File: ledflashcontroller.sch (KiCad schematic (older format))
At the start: 23 parts, among them J1 CONN_01X02, J2 CONN_01X02, J3 Conn_02x08_Odd_Even, K1 LDD-1000H, K2 LDD-1000H, P1 V_DIM1, P2 V_DIM2, P3 V_OUT, P4 I2C_HEADER, P5 GPIO_HEADER, P6 V_IN, Q1 IRLML6244, Q2 IRFB3256, U1 Teensy3.6

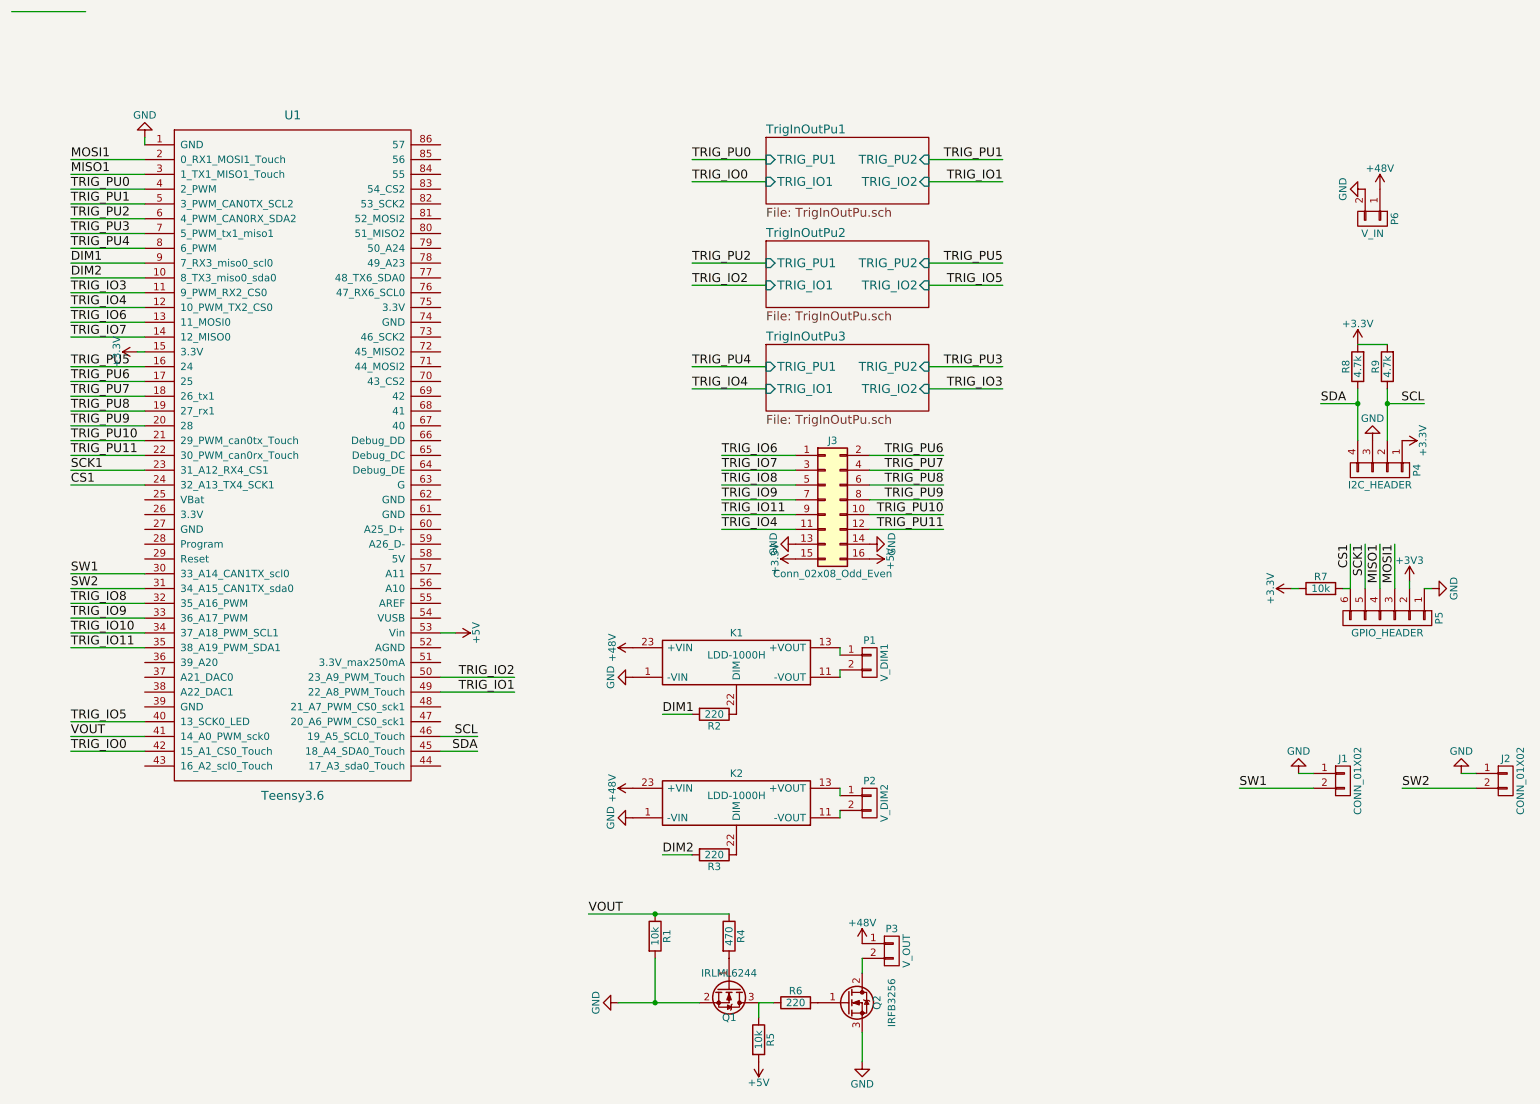
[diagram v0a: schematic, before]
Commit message: Fixed some annotations and footprints
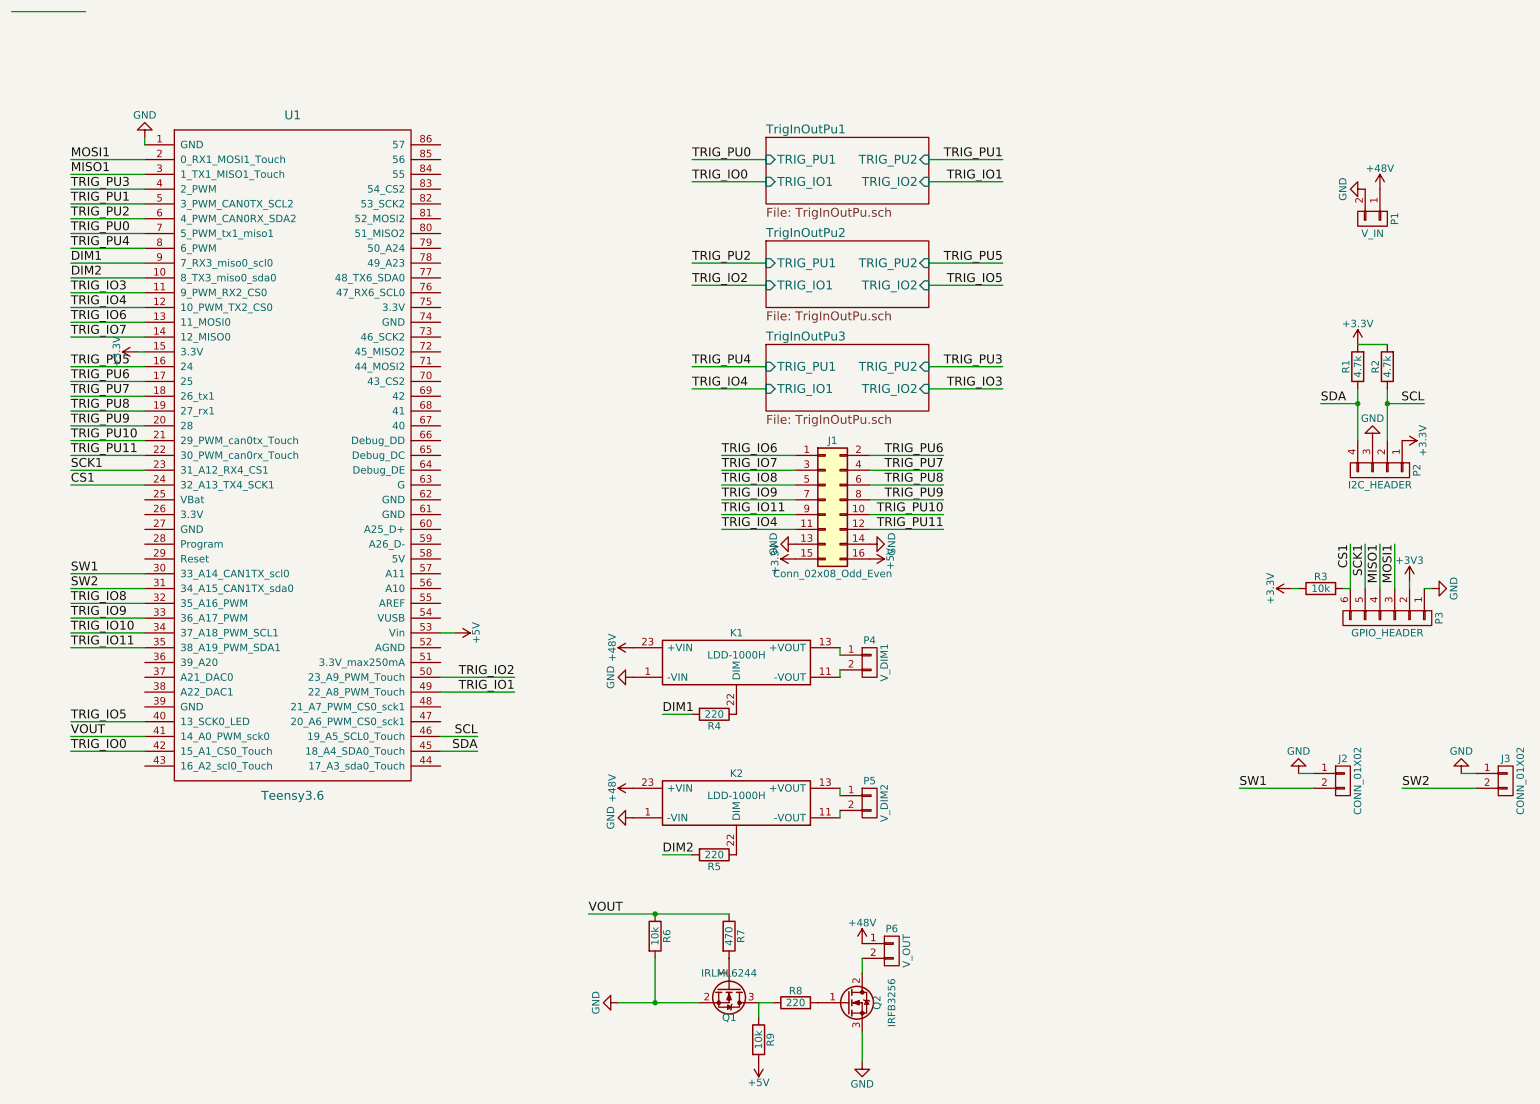
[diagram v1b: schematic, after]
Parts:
- J1: renamed from J3; footprint Pin_Headers:Pin_Header_Straight_2x08_Pitch1.00mm -> Pin_Headers:Pin_Header_Straight_2x08_Pitch2.54mm_SMD
- P3: renamed from P5; footprint Pin_Headers:Pin_Header_Straight_1x04_Pitch2.54mm -> Pin_Headers:Pin_Header_Straight_1x06_Pitch2.54mm
- renumbered J1 to J2, J2 to J3, P6 to P1, P4 to P2, P1 to P4, P2 to P5, P3 to P6, R8 to R1, R9 to R2, R7 to R3, R2 to R4, R3 to R5, R1 to R6, R4 to R7, R6 to R8, R5 to R9
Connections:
- net TRIG_PU0: now also U1.7 (5_PWM_tx1_miso1); no longer U1.4 (2_PWM)
- net TRIG_PU3: now also U1.4 (2_PWM); no longer U1.7 (5_PWM_tx1_miso1)
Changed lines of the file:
@@
 $EndComp
 $Comp
-L R R9
+L R R2
 U 1 1 5981ADF0
 P 9650 2450
-F 0 "R9" V 9730 2450 50  0000 C CNN
+F 0 "R2" V 9730 2450 50  0000 C CNN
 F 1 "4.7k" V 9650 2450 50  0000 C CNN
 F 2 "Resistors_SMD:R_1206_HandSoldering" V 9580 2450 50  0001 C CNN
@@
 $EndComp
 $Comp
-L R R8
+L R R1
 U 1 1 5981AE6C
 P 9450 2450
-F 0 "R8" V 9530 2450 50  0000 C CNN
+F 0 "R1" V 9530 2450 50  0000 C CNN
 F 1 "4.7k" V 9450 2450 50  0000 C CNN
 F 2 "Resistors_SMD:R_1206_HandSoldering" V 9380 2450 50  0001 C CNN
@@
 SCL
 $Comp
-L CONN_01X04 P4
+L CONN_01X04 P2
 U 1 1 5981B195
 P 9600 3150
-F 0 "P4" H 9600 3400 50  0000 C CNN
+F 0 "P2" H 9600 3400 50  0000 C CNN
 F 1 "I2C_HEADER" V 9700 3150 50  0000 C CNN
 F 2 "Pin_Headers:Pin_Header_Straight_1x04_Pitch2.54mm" H 9600 3150 50  0001 C CNN
@@
 SW2
 $Comp
-L CONN_01X02 P3
+L CONN_01X02 P6
 U 1 1 59820649
 P 6300 6400
-F 0 "P3" H 6300 6550 50  0000 C CNN
+F 0 "P6" H 6300 6550 50  0000 C CNN
 F 1 "V_OUT" V 6400 6400 50  0000 C CNN
 F 2 "lib_fp:DELTRON_571_x2" H 6300 6400 50  0001 C CNN
@@
 DIM1
 $Comp
-L CONN_01X02 P1
+L CONN_01X02 P4
 U 1 1 59824324
 P 6150 4450
-F 0 "P1" H 6150 4600 50  0000 C CNN
+F 0 "P4" H 6150 4600 50  0000 C CNN
 F 1 "V_DIM1" V 6250 4450 50  0000 C CNN
 F 2 "lib_fp:DELTRON_571_x2" H 6150 4450 50  0001 C CNN
@@
 DIM2
 $Comp
-L CONN_01X02 P2
+L CONN_01X02 P5
 U 1 1 5982447B
 P 6150 5400
-F 0 "P2" H 6150 5550 50  0000 C CNN
+F 0 "P5" H 6150 5550 50  0000 C CNN
 F 1 "V_DIM2" V 6250 5400 50  0000 C CNN
 F 2 "lib_fp:DELTRON_571_x2" H 6150 5400 50  0001 C CNN
@@
 CS1
 $Comp
-L CONN_01X06 P5
+L CONN_01X06 P3
 U 1 1 59825F8A
 P 9650 4150
-F 0 "P5" H 9650 4500 50  0000 C CNN
+F 0 "P3" H 9650 4500 50  0000 C CNN
 F 1 "GPIO_HEADER" V 9750 4150 50  0000 C CNN
-F 2 "Pin_Headers:Pin_Header_Straight_1x04_Pitch2.54mm" H 9650 4150 50  0001 C CNN
+F 2 "Pin_Headers:Pin_Header_Straight_1x06_Pitch2.54mm" H 9650 4150 50  0001 C CNN
 F 3 "" H 9650 4150 50  0000 C CNN
 	1    9650 4150
@@
 CS1
 $Comp
-L R R2
+L R R4
 U 1 1 5981D11F
 P 5100 4800
-F 0 "R2" V 5180 4800 50  0000 C CNN
+F 0 "R4" V 5180 4800 50  0000 C CNN
 F 1 "220" V 5100 4800 50  0000 C CNN
 F 2 "Resistors_SMD:R_1206_HandSoldering" V 5030 4800 50  0001 C CNN
@@
 $EndComp
 $Comp
-L CONN_01X02 P6
+L CONN_01X02 P1
 U 1 1 5992C559
 P 9550 1450
-F 0 "P6" H 9550 1600 50  0000 C CNN
+F 0 "P1" H 9550 1600 50  0000 C CNN
 F 1 "V_IN" V 9650 1450 50  0000 C CNN
 F 2 "lib_fp:DELTRON_571_x2" H 9550 1450 50  0001 C CNN
@@
 $EndComp
 $Comp
-L R R3
+L R R5
 U 1 1 5995EFDE
 P 5100 5750
-F 0 "R3" V 5180 5750 50  0000 C CNN
+F 0 "R5" V 5180 5750 50  0000 C CNN
 F 1 "220" V 5100 5750 50  0000 C CNN
 F 2 "Resistors_SMD:R_1206_HandSoldering" V 5030 5750 50  0001 C CNN
@@
 	5950 5450 5950 5500
 $Comp
-L R R1
+L R R6
 U 1 1 599C3A5A
 P 4700 6300
-F 0 "R1" V 4780 6300 50  0000 C CNN
+F 0 "R6" V 4780 6300 50  0000 C CNN
 F 1 "10k" V 4700 6300 50  0000 C CNN
 F 2 "Resistors_SMD:R_1206_HandSoldering" V 4630 6300 50  0001 C CNN
@@
 $EndComp
 $Comp
-L R R4
+L R R7
 U 1 1 599C3A60
 P 5200 6300
-F 0 "R4" V 5280 6300 50  0000 C CNN
+F 0 "R7" V 5280 6300 50  0000 C CNN
 F 1 "470" V 5200 6300 50  0000 C CNN
 F 2 "Resistors_SMD:R_1206_HandSoldering" V 5130 6300 50  0001 C CNN
@@
 $EndComp
 $Comp
-L R R5
+L R R9
 U 1 1 599C3A6D
 P 5400 7000
-F 0 "R5" V 5480 7000 50  0000 C CNN
+F 0 "R9" V 5480 7000 50  0000 C CNN
 F 1 "10k" V 5400 7000 50  0000 C CNN
 F 2 "Resistors_SMD:R_1206_HandSoldering" V 5330 7000 50  0001 C CNN
@@
 	4450 6750 5000 6750
 $Comp
-L R R6
+L R R8
 U 1 1 599C3A7D
 P 5650 6750
-F 0 "R6" V 5730 6750 50  0000 C CNN
+F 0 "R8" V 5730 6750 50  0000 C CNN
 F 1 "220" V 5650 6750 50  0000 C CNN
 F 2 "Resistors_SMD:R_1206_HandSoldering" V 5580 6750 50  0001 C CNN
@@
 	5400 6850 5400 6750
 $Comp
-L CONN_01X02 J1
+L CONN_01X02 J2
 U 1 1 59AA3763
 P 9350 5250
-F 0 "J1" H 9350 5400 50  0000 C CNN
+F 0 "J2" H 9350 5400 50  0000 C CNN
 F 1 "CONN_01X02" V 9450 5250 50  0000 C CNN
 F 2 "Pin_Headers:Pin_Header_Straight_1x02_Pitch2.54mm" H 9350 5250 50  0001 C CNN
@@
 $EndComp
 $Comp
-L CONN_01X02 J2
+L CONN_01X02 J3
 U 1 1 59AA3819
 P 10450 5250
-F 0 "J2" H 10450 5400 50  0000 C CNN
+F 0 "J3" H 10450 5400 50  0000 C CNN
 F 1 "CONN_01X02" V 10550 5250 50  0000 C CNN
 F 2 "Pin_Headers:Pin_Header_Straight_1x02_Pitch2.54mm" H 10450 5250 50  0001 C CNN
@@
 	9750 5300 10250 5300
 $Comp
-L R R7
+L R R3
 U 1 1 59AA62D1
 P 9200 3950
-F 0 "R7" V 9280 3950 50  0000 C CNN
+F 0 "R3" V 9280 3950 50  0000 C CNN
 F 1 "10k" V 9200 3950 50  0000 C CNN
 F 2 "Resistors_SMD:R_1206_HandSoldering" V 9130 3950 50  0001 C CNN
@@
 	1250 1450 750  1450
 Text Label 750  1250 0    60   ~ 0
-TRIG_PU0
+TRIG_PU3
 Text Label 750  1350 0    60   ~ 0
 TRIG_PU1
@@
 TRIG_PU2
 Text Label 750  1550 0    60   ~ 0
-TRIG_PU3
+TRIG_PU0
 Wire Wire Line
 	1250 1650 750  1650
@@
 TRIG_IO1
 $Comp
-L Conn_02x08_Odd_Even J3
+L Conn_02x08_Odd_Even J1
 U 1 1 59B82D2A
 P 5850 3350
-F 0 "J3" H 5900 3750 50  0000 C CNN
+F 0 "J1" H 5900 3750 50  0000 C CNN
 F 1 "Conn_02x08_Odd_Even" H 5900 2850 50  0000 C CNN
-F 2 "Pin_Headers:Pin_Header_Straight_2x08_Pitch1.00mm" H 5850 3350 50  0001 C CNN
+F 2 "Pin_Headers:Pin_Header_Straight_2x08_Pitch2.54mm_SMD" H 5850 3350 50  0001 C CNN
 F 3 "" H 5850 3350 50  0001 C CNN
 	1    5850 3350

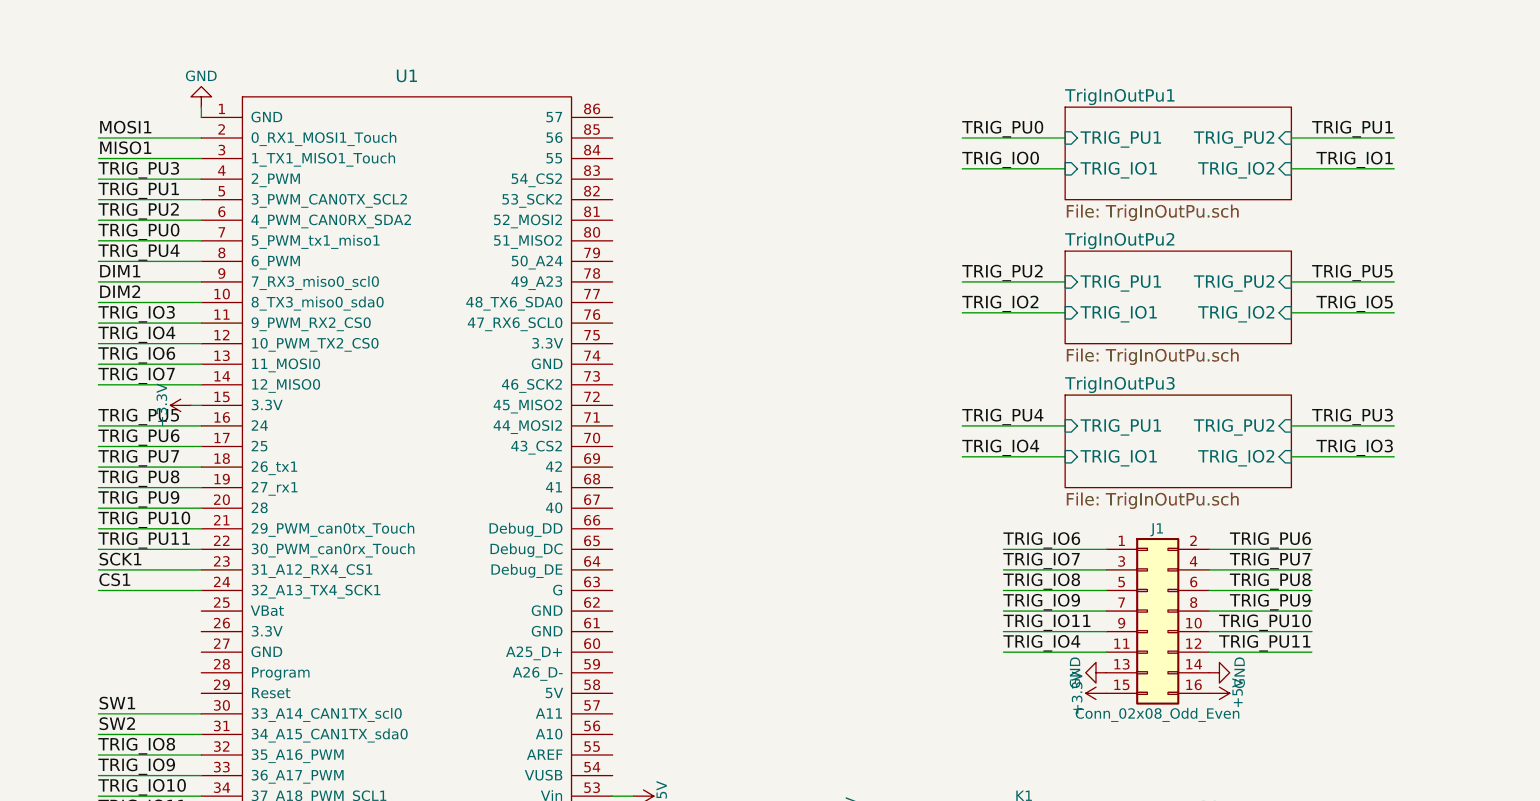
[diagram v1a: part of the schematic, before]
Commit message: Bugfixes for vias to close to wires
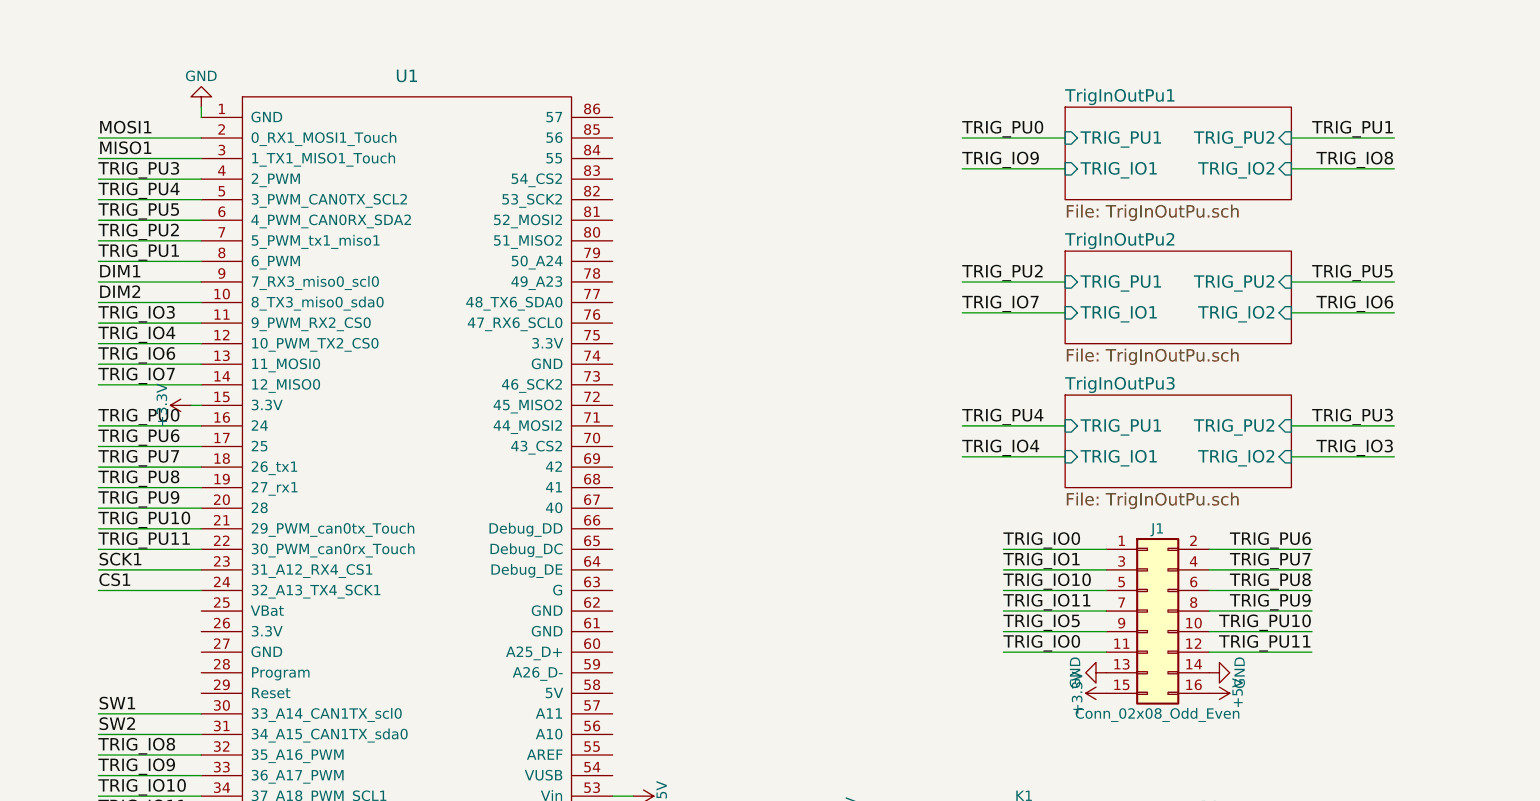
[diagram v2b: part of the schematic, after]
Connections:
- net TRIG_IO0: now also J1.1 (Pin_1), J1.11 (Pin_11)
- net TRIG_IO1: now also J1.3 (Pin_3)
- net TRIG_IO10: now also J1.5 (Pin_5)
- net TRIG_IO11: now also J1.7 (Pin_7); no longer J1.9 (Pin_9)
- net TRIG_IO4: no longer J1.11 (Pin_11)
- net TRIG_IO5: now also J1.9 (Pin_9)
- net TRIG_IO6: no longer J1.1 (Pin_1)
- net TRIG_IO7: no longer J1.3 (Pin_3)
- net TRIG_IO8: no longer J1.5 (Pin_5)
- net TRIG_IO9: no longer J1.7 (Pin_7)
- net TRIG_PU0: now also U1.16 (24); no longer U1.7 (5_PWM_tx1_miso1)
- net TRIG_PU1: now also U1.8 (6_PWM); no longer U1.5 (3_PWM_CAN0TX_SCL2)
- net TRIG_PU2: now also U1.7 (5_PWM_tx1_miso1); no longer U1.6 (4_PWM_CAN0RX_SDA2)
- net TRIG_PU4: now also U1.5 (3_PWM_CAN0TX_SCL2); no longer U1.8 (6_PWM)
- net TRIG_PU5: now also U1.6 (4_PWM_CAN0RX_SDA2); no longer U1.16 (24)
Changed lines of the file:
@@
 TRIG_PU3
 Text Label 750  1350 0    60   ~ 0
-TRIG_PU1
+TRIG_PU4
 Text Label 750  1450 0    60   ~ 0
+TRIG_PU5
+Text Label 750  1550 0    60   ~ 0
 TRIG_PU2
-Text Label 750  1550 0    60   ~ 0
-TRIG_PU0
 Wire Wire Line
 	1250 1650 750  1650
 Text Label 750  1650 0    60   ~ 0
-TRIG_PU4
+TRIG_PU1
 Wire Wire Line
 	1250 2750 750  2750
@@
 	1250 2650 750  2650
 Text Label 750  2450 0    60   ~ 0
-TRIG_PU5
+TRIG_PU0
 Text Label 750  2550 0    60   ~ 0
 TRIG_PU6
@@
 	5450 1200 4950 1200
 Text Label 4950 1200 0    60   ~ 0
-TRIG_IO0
+TRIG_IO9
 Wire Wire Line
 	5450 1900 4950 1900
 Text Label 4950 1900 0    60   ~ 0
-TRIG_IO2
+TRIG_IO7
 Wire Wire Line
 	5450 2600 4950 2600
@@
 	6550 1900 7050 1900
 Text Label 7050 1900 2    60   ~ 0
-TRIG_IO5
+TRIG_IO6
 Wire Wire Line
 	6550 1200 7050 1200
 Text Label 7050 1200 2    60   ~ 0
-TRIG_IO1
+TRIG_IO8
 $Comp
 L Conn_02x08_Odd_Even J1
@@
 	5650 3550 5150 3550
 Text Label 5150 3550 0    60   ~ 0
-TRIG_IO4
+TRIG_IO0
 Wire Wire Line
 	5650 3450 5150 3450
 Text Label 5150 3450 0    60   ~ 0
-TRIG_IO11
+TRIG_IO5
 Wire Wire Line
 	5650 3350 5150 3350
 Text Label 5150 3350 0    60   ~ 0
-TRIG_IO9
+TRIG_IO11
 Wire Wire Line
 	5650 3250 5150 3250
 Text Label 5150 3250 0    60   ~ 0
-TRIG_IO8
+TRIG_IO10
 Wire Wire Line
 	5650 3150 5150 3150
 Text Label 5150 3150 0    60   ~ 0
-TRIG_IO7
+TRIG_IO1
 Wire Wire Line
 	5650 3050 5150 3050
 Text Label 5150 3050 0    60   ~ 0
-TRIG_IO6
+TRIG_IO0
 Wire Wire Line
 	6150 3050 6650 3050
